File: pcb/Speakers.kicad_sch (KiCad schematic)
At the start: 34 parts, among them U4 ADA4891, U7 ADA4891

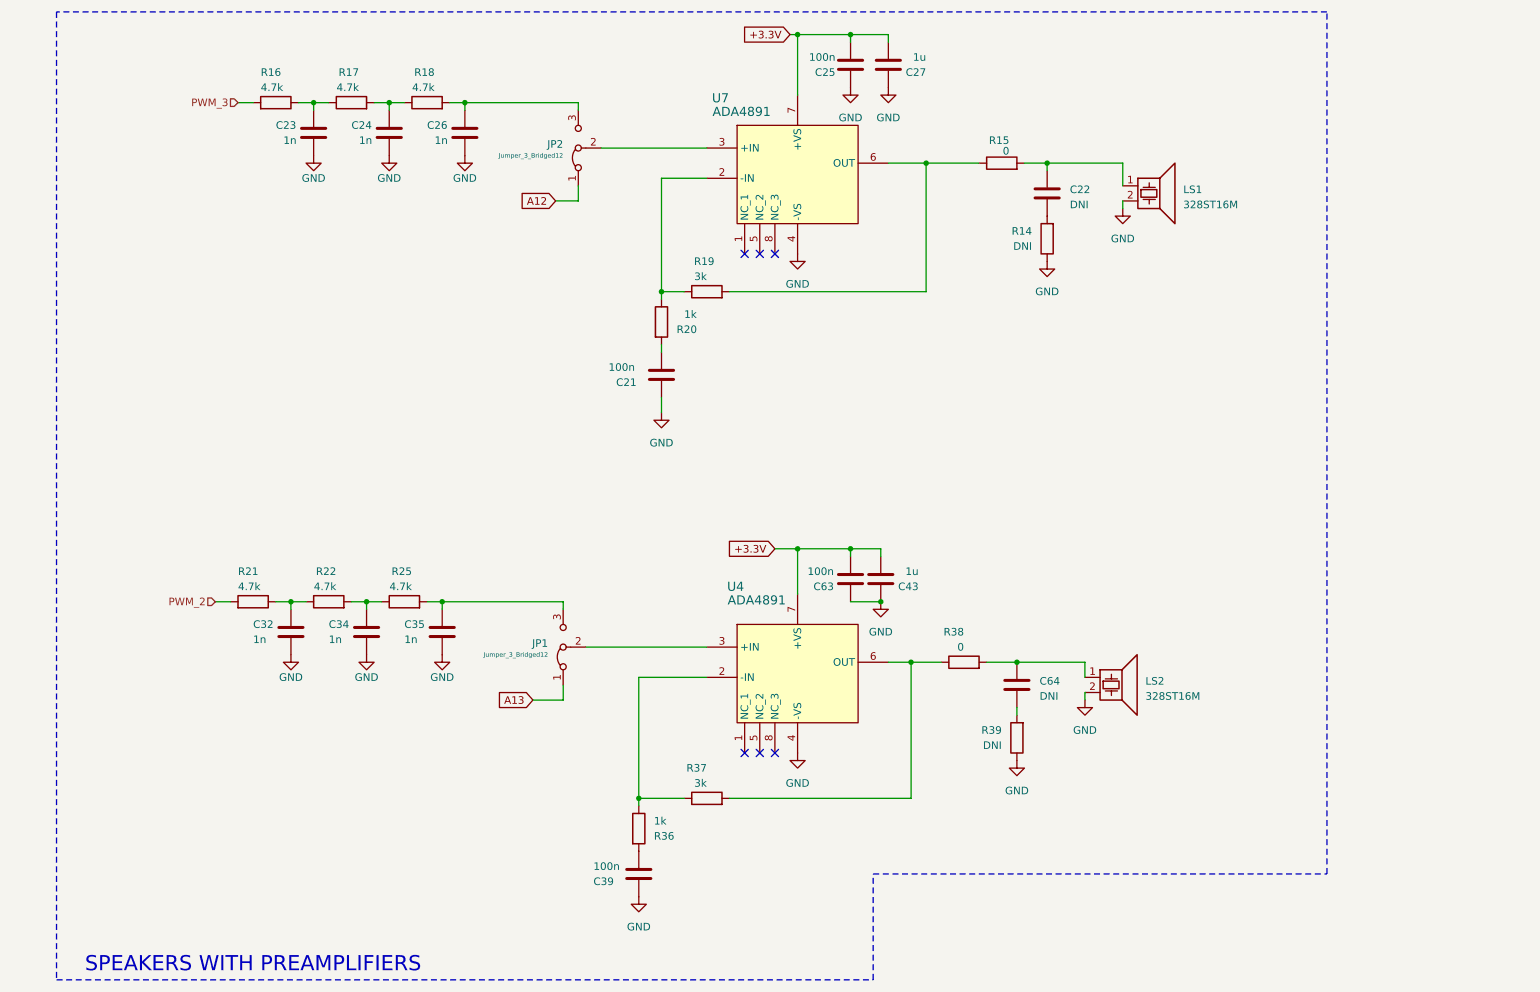
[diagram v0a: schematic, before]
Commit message: pcb: New PCB revision (#88)
- Rearrange schematics
- Better symbols and footprints
- Better names and graphics
- Add simulations for DC offset after AC coupling
- Add BOM
- Redraw PCB layout
- Proper position for pressure and humidity sensor
- Better positions for EXT headers
- Silkscreen text labels for headers, pins, mics, etc.
- Change supply polarity and pin numbers of ADA4511
- Change cap of switches to 100n to reduce BOM
- Change supply of sensors to unison 3.3V
- Rearrange ADC pins
- Add digital switches instead of manual headers
- Add logos

---------

Co-authored-by: oberfeli <felix.ober@mailbox.org>
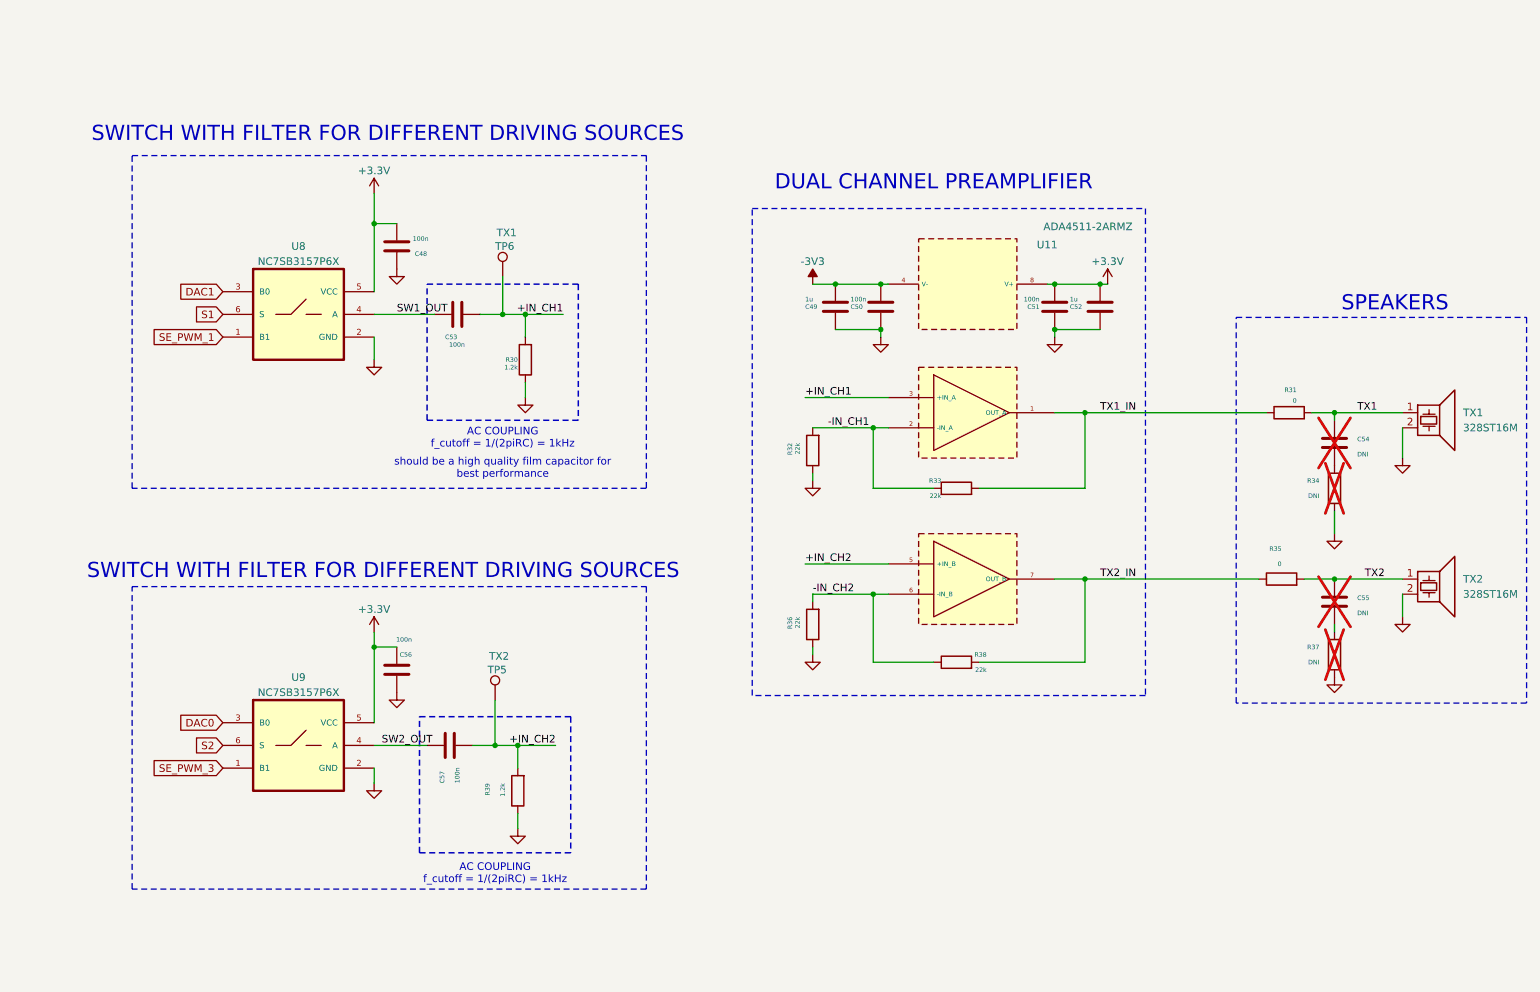
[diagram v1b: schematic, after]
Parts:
- removed C21, C25, C39, C63: 100n, Capacitor_SMD:C_0805_2012Metric, symbol Device:C
- removed C23, C24, C26, C32, C34, C35: 1n, Capacitor_SMD:C_0805_2012Metric, symbol Device:C
- removed C27, C43: 1u, Capacitor_SMD:C_0805_2012Metric, symbol Device:C
- removed JP1, JP2: Jumper_3_Bridged12, Connector_PinHeader_2.54mm:PinHeader_1x03_P2.54mm_Vertical, symbol Jumper:Jumper_3_Bridged12
- removed R16, R17, R18, R21, R22, R25: 4.7k, Resistor_SMD:R_0805_2012Metric, symbol Device:R
- removed R19, R37: 3k, Resistor_SMD:R_0805_2012Metric, symbol Device:R
- removed R20, R36: 1k, Resistor_SMD:R_0805_2012Metric, symbol Device:R
- removed U4, U7: ADA4891, SensEdu:ADA4891-1ARZ, symbol SensEdu:ADA4891-1ARZ
- added C48, C50, C51, C53, C56, C57: 100n, Capacitor_SMD:C_0603_1608Metric, symbol SensEdu:C
- added C49, C52: 1u, Capacitor_SMD:C_0603_1608Metric, symbol SensEdu:C
- added R30, R39: 1.2k, Resistor_SMD:R_0603_1608Metric, symbol SensEdu:R
- added R32, R33, R36, R38: 22k, Resistor_SMD:R_0603_1608Metric, symbol SensEdu:R
- added TP5: TX2, TestPoint:TestPoint_THTPad_D2.0mm_Drill1.0mm, symbol SensEdu:TestPoint
- added TP6: TX1, TestPoint:TestPoint_THTPad_D2.0mm_Drill1.0mm, symbol SensEdu:TestPoint
- added U11: ADA4511-2ARMZ, SamacSys_Parts:SOP65P490X110-8N, symbol SensEdu:ADA4511-2ARMZ
- added U8, U9: NC7SB3157P6X, SensEdu:SOT65P210X110-6N, symbol SensEdu:NC7SB3157P6X
- C54: renamed from C22; footprint Capacitor_SMD:C_0805_2012Metric -> Capacitor_SMD:C_0603_1608Metric; symbol Device:C -> SensEdu:C; now not fitted
- C55: renamed from C64; footprint Capacitor_SMD:C_0805_2012Metric -> Capacitor_SMD:C_0603_1608Metric; symbol Device:C -> SensEdu:C; now not fitted
- R31: renamed from R15; footprint Resistor_SMD:R_0805_2012Metric -> Resistor_SMD:R_0603_1608Metric; symbol Device:R -> SensEdu:R
- R34: renamed from R14; footprint Resistor_SMD:R_0805_2012Metric -> Resistor_SMD:R_0603_1608Metric; symbol Device:R -> SensEdu:R; now not fitted
- R35: renamed from R38; footprint Resistor_SMD:R_0805_2012Metric -> Resistor_SMD:R_0603_1608Metric; symbol Device:R -> SensEdu:R
- R37: renamed from R39; footprint Resistor_SMD:R_0805_2012Metric -> Resistor_SMD:R_0603_1608Metric; symbol Device:R -> SensEdu:R; now not fitted
- TX1: renamed from LS1; symbol Device:Speaker_Ultrasound -> SensEdu:Speaker_Ultrasound
- TX2: renamed from LS2; symbol Device:Speaker_Ultrasound -> SensEdu:Speaker_Ultrasound
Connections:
- net +3.3V: now also C48.2, C51.2, C52.1, C56.2, U11.8 (V+), U8.5 (VCC), U9.5 (VCC)
- net GND: now also C48.1, C49.2, C50.2, C51.1, C52.2, C56.1, R30.1, R32.1, R36.1, R39.1, U8.2 (GND), U9.2 (GND)
- net TX1_IN: now reaches R31.1
- net TX1_IN: now also R33.2, U11.1 (OUT_A)
- net TX2: now reaches C55.1, R35.2, TX2.1
- net TX1: now reaches C54.1, R31.2, TX1.1
- net TX2_IN: now reaches R35.1
- net TX2_IN: now also R38.2, U11.7 (OUT_B)
- new net +IN_CH1: C53.2, R30.2, TP6.1, U11.3 (+IN_A)
- new net +IN_CH2: C57.2, R39.2, TP5.1, U11.5 (+IN_B)
- new net -3V3: C49.1, C50.1, U11.4 (V-)
- new net -IN_CH1: R32.2, R33.1, U11.2 (-IN_A)
- new net -IN_CH2: R36.2, R38.1, U11.6 (-IN_B)
- new net DAC0: U9.3 (B0)
- new net DAC1: U8.3 (B0)
- new net S1: U8.6 (S)
- new net S2: U9.6 (S)
- new net SE_PWM_1: U8.1 (B1)
- new net SE_PWM_3: U9.1 (B1)
- new net SW1_OUT: C53.1, U8.4 (A)
- new net SW2_OUT: C57.1, U9.4 (A)
- no-connect marks 6 -> 0
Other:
- note added: "AC COUPLING f_cutoff = 1/(2piRC) = 1kHz"
- note added: "DUAL CHANNEL PREAMPLIFIER"
- note added: "SPEAKERS"
- note added: "SWITCH WITH FILTER FOR DIFFERENT DRIVING SOURCES"
- note added: "should be a high quality film capacitor for best performance"
- note removed: "SPEAKERS WITH PREAMPLIFIERS"
- title: SensEdu 0.7 -> SensEdu
- moved on the sheet: R31, R35, TX1, TX2
